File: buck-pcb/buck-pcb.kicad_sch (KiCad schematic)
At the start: 10 parts

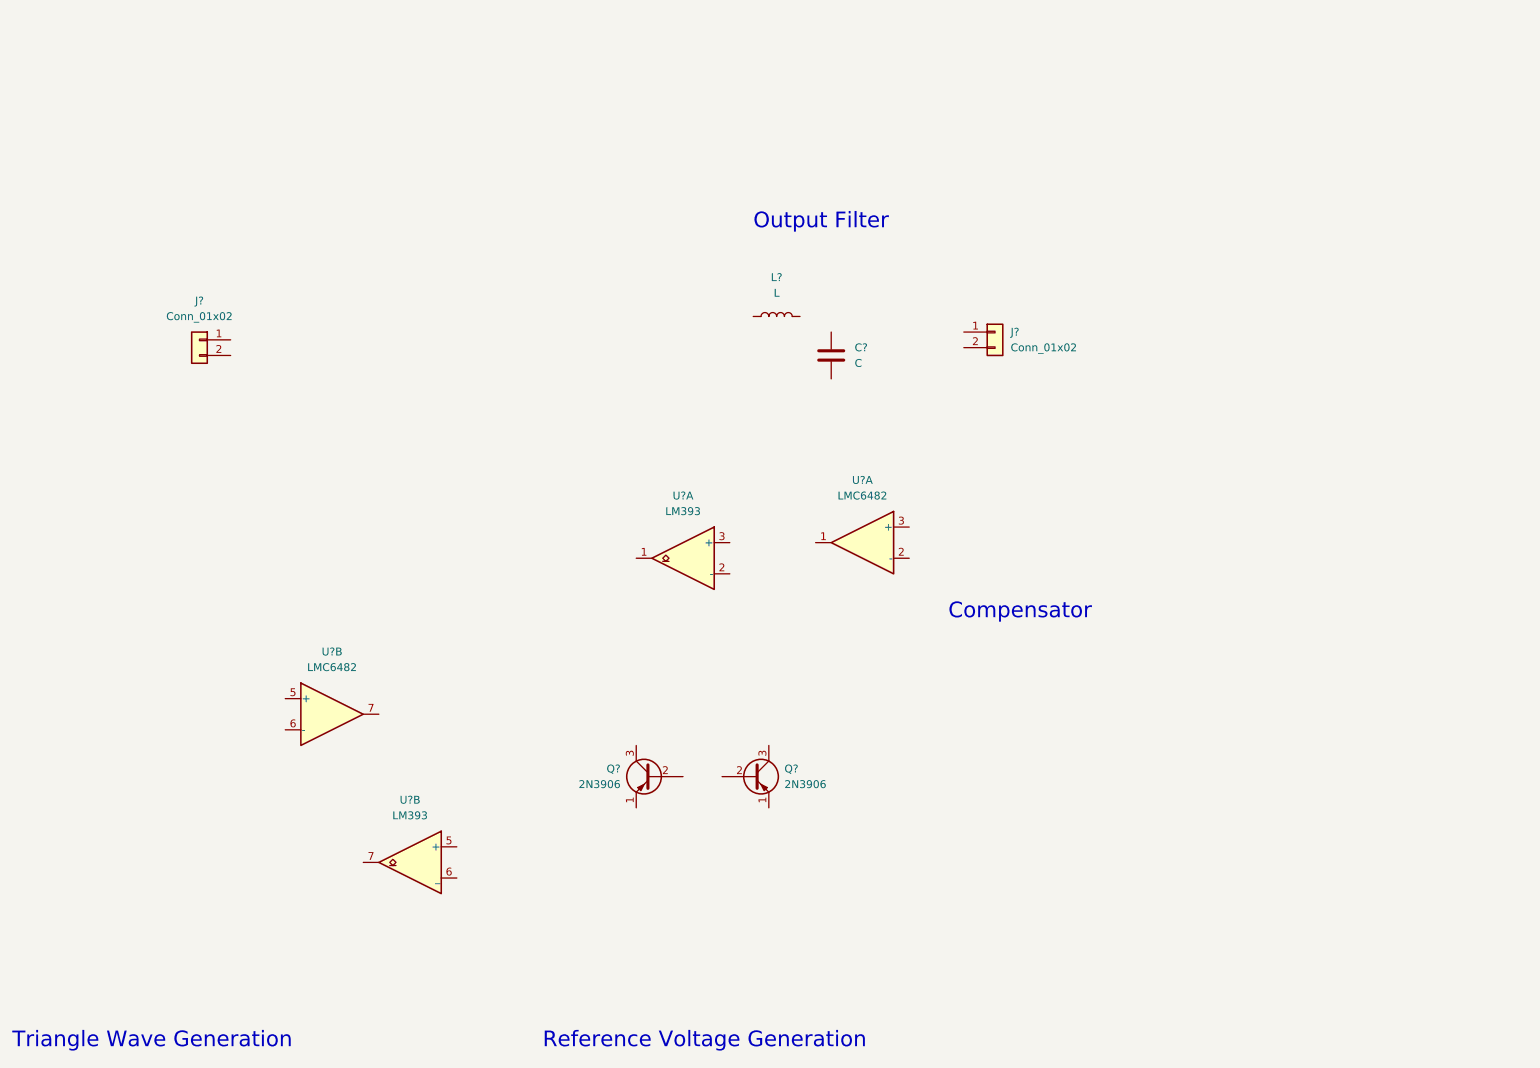
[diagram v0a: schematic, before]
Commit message: KiCAD schematic mostly done
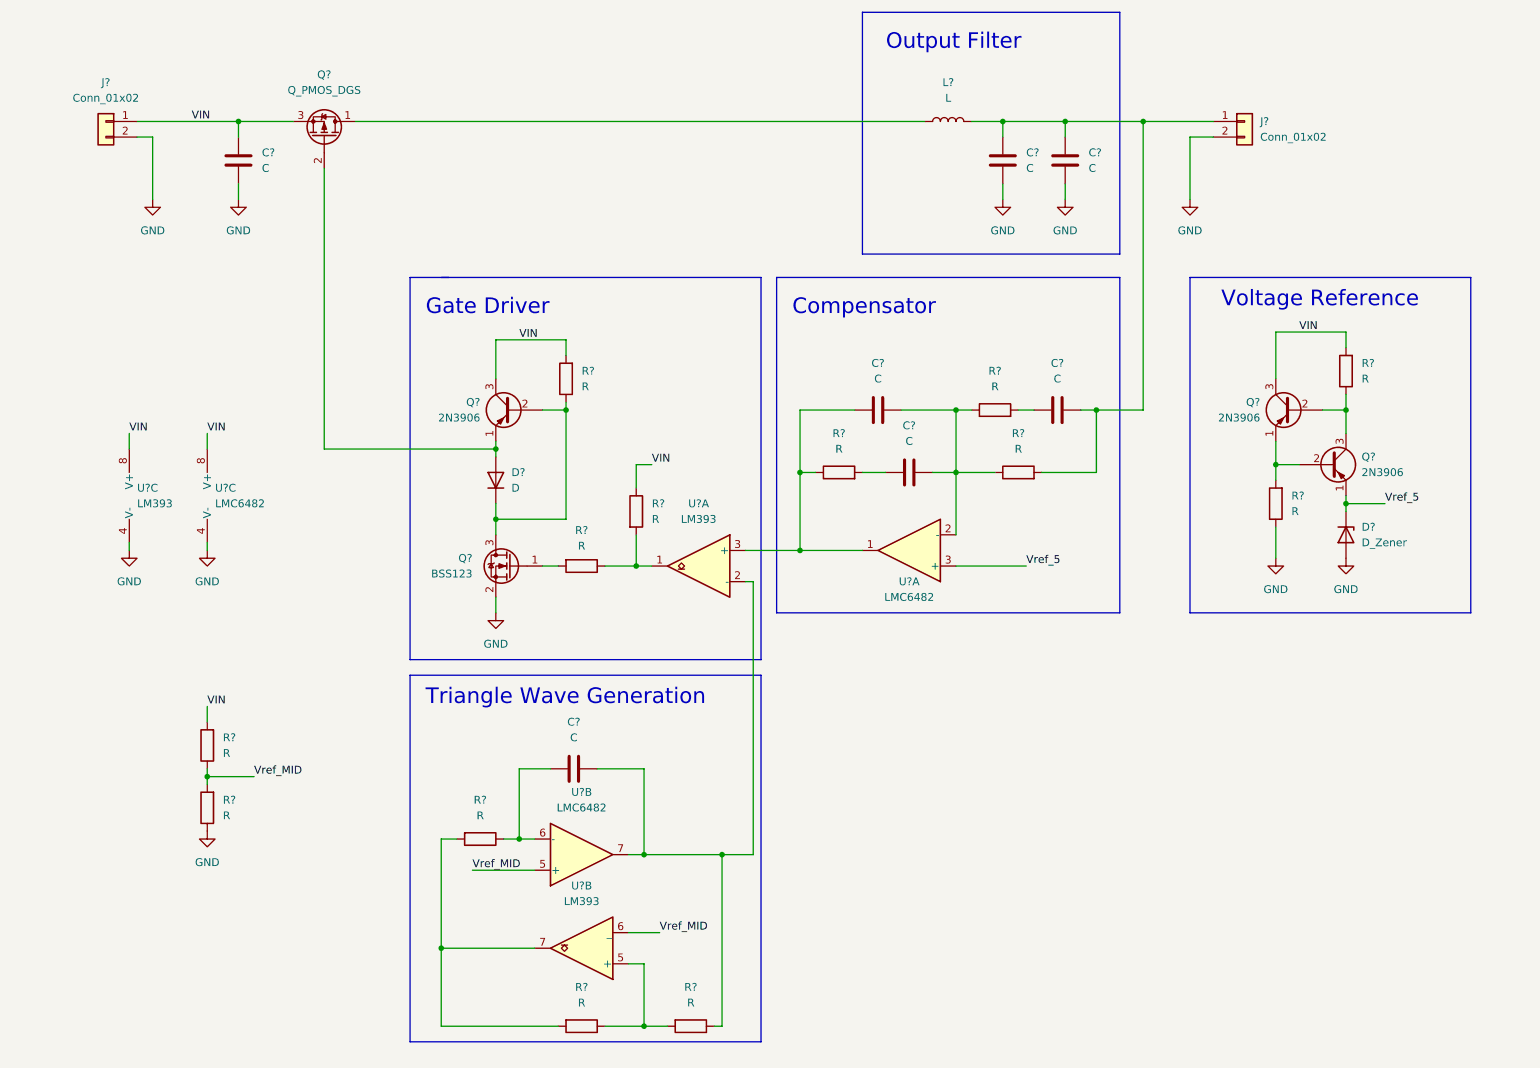
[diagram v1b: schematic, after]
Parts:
- removed Q? (x2): 2N3906, Package_TO_SOT_THT:TO-92_Inline, symbol Transistor_BJT:2N3906
- added C? (x6): C, symbol Device:C
- added D?: D_Zener, symbol Device:D_Zener
- added D?: D, symbol Device:D
- added Q? (x3): 2N3906, Package_TO_SOT_THT:TO-92_Inline, symbol Transistor_BJT:2N3906
- added Q?: Q_PMOS_DGS, symbol Device:Q_PMOS_DGS
- added Q?: BSS123, Package_TO_SOT_SMD:SOT-23, symbol Transistor_FET:BSS123
- added R? (x13): R, symbol Device:R
- added U?: LMC6482, symbol Amplifier_Operational:LMC6482
- added U?: LM393, symbol Comparator:LM393
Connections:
- net Vref_MID: now reaches U?.5 (+)
- net Vref_MID: now also U?.6 (_), R?.1, R?.2
- net at U?.6 (-): now also C?.1, R?.1
- net at U?.7: now also U?.2 (-), C?.2, R?.1
- net at U?.5 (+): now also R?.1, R?.2
- net at U?.7: now also R?.2, R?.2
- net at L?.1: now also Q?.1 (D)
- net at L?.2: now also C?.1, J?.1 (Pin_1), C?.1, C?.2, R?.2
- net at U?.1: now also U?.3 (+), C?.1, R?.1
- net at U?.2 (-): now also C?.2, C?.2, R?.1, R?.1
- net Vref_5: now reaches U?.3 (+)
- net Vref_5: now also D?.1 (K), Q?.1 (E)
- net GND: now reaches C?.2
- net GND: now also J?.2 (Pin_2), J?.2 (Pin_2), C?.2, C?.2, D?.2 (A), Q?.2 (S), R?.1, R?.1, U?.4 (V-), U?.4 (V-)
- net at U?.1: now also R?.1, R?.2
- net VIN: now reaches J?.1 (Pin_1)
- net VIN: now also C?.1, Q?.3 (C), Q?.3 (C), Q?.3 (S), R?.1, R?.2, R?.2, R?.2, U?.8 (V+), U?.8 (V+)
- new net: C?.1, R?.2 (x2)
- new net: Q?.1 (E), Q?.2 (B), R?.2
- new net: Q?.2 (B), Q?.3 (C), R?.1
- new net: D?.2 (A), Q?.1 (E), Q?.2 (G)
- new net: Q?.1 (G), R?.2
- new net: D?.1 (K), Q?.2 (B), Q?.3 (D), R?.1
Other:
- note added: "Gate Driver"
- note added: "Voltage Reference"
- note removed: "Reference Voltage Generation"
- moved on the sheet: C?, J?, L?, U?A, U?B

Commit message: Putting together complete system
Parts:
- added C? (x2): 0.1u, symbol Device:C
- added D?: D_Schottky, symbol Device:D_Schottky
- added R?: 270, symbol Device:R
- C1, C7: renamed from C?; value C -> 10u
- C2: renamed from C?; value C -> 200p
- C3: renamed from C?; value C -> 82p
- C4, C6: renamed from C?; value C -> 10n
- C5: renamed from C?; value C -> 100u
- R1, R12, R2, R8, R9: renamed from R?; value R -> 10k
- R10: renamed from R?; value R -> 680
- R11: renamed from R?; value R -> 27k
- R13: renamed from R?; value R -> 82
- R3: renamed from R?; value R -> 4.7k
- R4, R7: renamed from R?; value R -> 1k
- R5: renamed from R?; value R -> 33
- R6: renamed from R?; value R -> 20k
- gave numbers to parts that had none: 12
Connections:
- net GND: now also C?.2, C?.2, D?.2 (A)
- net VIN: now also C?.1, C?.1, R?.1
- net at L1.1, Q1.1 (D): now also D?.1 (K)
- net at R3.2, R6.2, U1.7: now also R?.2
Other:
- moved on the sheet: C2, C5, C7, L1, R1, R2, R3, R6, R8, U1B, U1C, U2B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

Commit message: FP assigned
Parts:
- removed Q1: Q_PMOS_DGS, symbol Device:Q_PMOS_DGS
- removed Q2, Q4, Q5: 2N3906, Package_TO_SOT_THT:TO-92_Inline, symbol Transistor_BJT:2N3906
- added D4: LED, LED_SMD:LED_0603_1608Metric, symbol Device:LED
- added Q1: Q_PMOS_GSD, Package_TO_SOT_SMD:SOT-23, symbol Device:Q_PMOS_GSD
- added Q2, Q4, Q5: MMBT3906, Package_TO_SOT_SMD:SOT-23, symbol Transistor_BJT:MMBT3906
- added R15: 270, Resistor_SMD:R_0603_1608Metric, symbol Device:R
- C1, C2, C3, C4, C6, C7: footprint (none) -> Capacitor_SMD:C_0603_1608Metric
- C5: footprint (none) -> Capacitor_THT:CP_Radial_D8.0mm_P3.50mm
- C8, C9: renamed from C?; footprint (none) -> Capacitor_SMD:C_0603_1608Metric
- D1: value D -> 1N4148; footprint (none) -> Diode_SMD:D_SOD-323_HandSoldering
- D2: footprint (none) -> Diode_THT:D_DO-41_SOD81_P7.62mm_Horizontal
- D3: renamed from D?; footprint (none) -> Diode_SMD:D_SMB
- J1, J2: footprint (none) -> Connector_PinHeader_2.54mm:PinHeader_1x02_P2.54mm_Vertical
- L1: value L -> 10u; footprint (none) -> Inductor_SMD:L_7.3x7.3_H3.5
- R1, R10, R11, R12, R13, R2, R3, R4, R5, R6, R7, R8, R9: footprint (none) -> Resistor_SMD:R_0603_1608Metric
- R14: renamed from R?; footprint (none) -> Resistor_SMD:R_0603_1608Metric
- U1, U2: footprint (none) -> Package_SO:SOIC-8_3.9x4.9mm_P1.27mm
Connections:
- net GND: now also D4.1 (K)
- net VIN: now also Q1.2 (S), Q2.3 (C), Q4.3 (C)
- net Vref_5: now also Q5.2 (E)
- net at C5.1, C6.2, C7.1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: now also R15.1
- net at R12.2: now also Q4.2 (E), Q5.1 (B)
- net at R13.1: now also Q4.1 (B), Q5.3 (C)
- net at D3.1 (K), L1.1: now also Q1.3 (D)
- net at D1.2 (A): now also Q1.1 (G), Q2.2 (E)
- net at D1.1 (K), Q3.3 (D), R4.1: now also Q2.1 (B)
- new net: D4.2 (A), R15.2
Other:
- moved on the sheet: J2

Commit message: Initial layout
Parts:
- added C10: 0.1u, Capacitor_SMD:C_0603_1608Metric, symbol Device:C
- D2: footprint Diode_THT:D_DO-41_SOD81_P7.62mm_Horizontal -> Diode_SMD:D_SOD-123
- L1: footprint Inductor_SMD:L_7.3x7.3_H3.5 -> buck-graphics:BMRx00060630
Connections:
- net GND: now also C10.2
- net Vref_5: now also U2.5 (+); no longer U2.3 (+)
- net Vref_MID: now also U2.3 (+), C10.1; no longer U2.5 (+)
- net VOUT: now reaches C5.1, C6.2, C7.1, J2.1 (Pin_1), L1.2, R11.2, R15.1
- net at C3.2, C4.2, R10.1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: now also U2.6 (-); no longer U2.2 (-)
- net at C3.1, R9.1, U1.3 (+): now also U2.7; no longer U2.1
- net at C2.1, R3.1: now also U2.2 (-); no longer U2.6 (-)
- net at C2.2, R8.1, U1.2 (-): now also U2.1; no longer U2.7
- net VSW: now reaches D3.1 (K), L1.1, Q1.3 (D)
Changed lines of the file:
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@@
   (junction (at 234.95 102.87) (diameter 0) (color 0 0 0 0)
   )
+  (junction (at 50.8 152.4) (diameter 0) (color 0 0 0 0)
+  )
   (junction (at 96.52 105.41) (diameter 0) (color 0 0 0 0)
   )
@@
     (stroke (width 0) (type default) (color 0 0 0 0))
   )
+  (wire (pts (xy 50.8 152.4) (xy 39.37 152.4))
+    (stroke (width 0) (type default) (color 0 0 0 0))
+  )
   (wire (pts (xy 96.52 105.41) (xy 96.52 107.95))
     (stroke (width 0) (type default) (color 0 0 0 0))
@@
     (stroke (width 0) (type default) (color 0 0 0 0))
   )
+  (wire (pts (xy 50.8 152.4) (xy 50.8 153.67))
+    (stroke (width 0) (type default) (color 0 0 0 0))
+  )
   (wire (pts (xy 201.93 40.64) (xy 201.93 87.63))
     (stroke (width 0) (type default) (color 0 0 0 0))
@@
     (stroke (width 0) (type default) (color 0 0 0 0))
   )
-  (wire (pts (xy 46.99 152.4) (xy 39.37 152.4))
+  (wire (pts (xy 53.34 152.4) (xy 50.8 152.4))
     (stroke (width 0) (type default) (color 0 0 0 0))
   )
@@
     (effects (font (size 2.54 2.54)) (justify left bottom))
   )
+  (label "VSW" (at 120.65 40.64 0)
+    (effects (font (size 1.27 1.27)) (justify left bottom))
+  )
   (label "VIN" (at 33.02 105.41 0)
     (effects (font (size 1.27 1.27)) (justify left bottom))
@@
     (effects (font (size 1.27 1.27)) (justify left bottom))
   )
+  (label "VOUT" (at 227.33 40.64 0)
+    (effects (font (size 1.27 1.27)) (justify left bottom))
+  )
   (label "VIN" (at 39.37 140.97 0)
     (effects (font (size 1.27 1.27)) (justify left bottom))
@@
     (effects (font (size 1.27 1.27)) (justify left bottom))
   )
-  (label "Vref_MID" (at 46.99 152.4 0)
+  (label "Vref_MID" (at 53.34 152.4 0)
     (effects (font (size 1.27 1.27)) (justify left bottom))
   )
@@
     (pin "2")
   )
+  (symbol (lib_id "Device:C") (at 50.8 157.48 0) (unit 1)
+    (in_bom yes) (on_board yes) (fields_autoplaced)
+    (property "Reference" "C10" (id 0) (at 54.61 156.2099 0)
+      (effects (font (size 1.27 1.27)) (justify left))
+    )
+    (property "Value" "0.1u" (id 1) (at 54.61 158.7499 0)
+      (effects (font (size 1.27 1.27)) (justify left))
+    )
+    (property "Footprint" "Capacitor_SMD:C_0603_1608Metric" (id 2) (at 51.7652 161.29 0)
+      (effects (font (size 1.27 1.27)) hide)
+    )
+    (property "Datasheet" "~" (id 3) (at 50.8 157.48 0)
+      (effects (font (size 1.27 1.27)) hide)
+    )
+    (pin "1")
+    (pin "2")
+  )
   (symbol (lib_id "Device:C") (at 187.96 46.99 0) (unit 1)
     (in_bom yes) (on_board yes) (fields_autoplaced)
@@
     (pin "1")
   )
-  (symbol (lib_id "Amplifier_Operational:LMC6482") (at 110.49 161.29 0) (mirror x) (unit 2)
+  (symbol (lib_id "Amplifier_Operational:LMC6482") (at 110.49 161.29 0) (mirror x) (unit 1)
     (in_bom yes) (on_board yes)
     (property "Reference" "U2" (id 0) (at 114.3 153.67 0))
@@
       (effects (font (size 1.27 1.27)) hide)
     )
-    (pin "5")
-    (pin "6")
-    (pin "7")
+    (pin "1")
+    (pin "2")
+    (pin "3")
   )
   (symbol (lib_id "power:GND") (at 54.61 53.34 0) (unit 1)
@@
     (property "Reference" "L1" (id 0) (at 166.37 34.29 90))
     (property "Value" "10u" (id 1) (at 166.37 36.83 90))
-    (property "Footprint" "Inductor_SMD:L_7.3x7.3_H3.5" (id 2) (at 166.37 40.64 0)
+    (property "Footprint" "buck-graphics:BMRx00060630" (id 2) (at 166.37 40.64 0)
       (effects (font (size 1.27 1.27)) hide)
     )
@@
     (pin "1")
   )
-  (symbol (lib_id "Amplifier_Operational:LMC6482") (at 163.83 110.49 180) (unit 1)
+  (symbol (lib_id "Amplifier_Operational:LMC6482") (at 163.83 110.49 180) (unit 2)
     (in_bom yes) (on_board yes)
     (property "Reference" "U2" (id 0) (at 163.83 115.57 0))
@@
       (effects (font (size 1.27 1.27)) hide)
     )
-    (pin "1")
-    (pin "2")
-    (pin "3")
+    (pin "5")
+    (pin "6")
+    (pin "7")
   )
   (symbol (lib_id "power:GND") (at 46.99 118.11 0) (unit 1)
@@
     (pin "2")
   )
+  (symbol (lib_id "power:GND") (at 50.8 161.29 0) (unit 1)
+    (in_bom yes) (on_board yes) (fields_autoplaced)
+    (property "Reference" "#PWR0101" (id 0) (at 50.8 167.64 0)
+      (effects (font (size 1.27 1.27)) hide)
+    )
+    (property "Value" "GND" (id 1) (at 50.8 166.37 0))
+    (property "Footprint" "" (id 2) (at 50.8 161.29 0)
+      (effects (font (size 1.27 1.27)) hide)
+    )
+    (property "Datasheet" "" (id 3) (at 50.8 161.29 0)
+      (effects (font (size 1.27 1.27)) hide)
+    )
+    (pin "1")
+  )
   (symbol (lib_id "power:GND") (at 33.02 118.11 0) (unit 1)
     (in_bom yes) (on_board yes) (fields_autoplaced)
@@
       (effects (font (size 1.27 1.27)) (justify left))
     )
-    (property "Footprint" "Diode_THT:D_DO-41_SOD81_P7.62mm_Horizontal" (id 2) (at 234.95 107.95 0)
+    (property "Footprint" "Diode_SMD:D_SOD-123" (id 2) (at 234.95 107.95 0)
       (effects (font (size 1.27 1.27)) hide)
     )
@@
       (reference "#PWR015") (unit 1) (value "GND") (footprint "")
     )
+    (path "/cd9f7193-c134-4e35-b550-bcfe2155c88e"
+      (reference "#PWR0101") (unit 1) (value "GND") (footprint "")
+    )
     (path "/30d31727-8e0f-449d-aa6e-ffb0c66bd448"
       (reference "C1") (unit 1) (value "10u") (footprint "Capacitor_SMD:C_0603_1608Metric")
@@
       (reference "C9") (unit 1) (value "0.1u") (footprint "Capacitor_SMD:C_0603_1608Metric")
     )
+    (path "/207f3b04-5d05-4d5e-a65c-613b60a18274"
+      (reference "C10") (unit 1) (value "0.1u") (footprint "Capacitor_SMD:C_0603_1608Metric")
+    )
     (path "/eb146731-2879-4699-bc00-e8e6010b77ab"
       (reference "D1") (unit 1) (value "1N4148") (footprint "Diode_SMD:D_SOD-323_HandSoldering")
     )
     (path "/d7ea3f33-f308-4721-81bb-746244b64807"
-      (reference "D2") (unit 1) (value "D_Zener") (footprint "Diode_THT:D_DO-41_SOD81_P7.62mm_Horizontal")
+      (reference "D2") (unit 1) (value "D_Zener") (footprint "Diode_SMD:D_SOD-123")
     )
     (path "/aae01ab9-176d-45dc-8846-cc715be406a0"
@@
     )
     (path "/7a7be03b-d30a-4fc6-abe7-e94916bf3a0b"
-      (reference "L1") (unit 1) (value "10u") (footprint "Inductor_SMD:L_7.3x7.3_H3.5")
+      (reference "L1") (unit 1) (value "10u") (footprint "buck-graphics:BMRx00060630")
     )
     (path "/c70c6b42-076d-480e-b33c-459aff21d426"
@@
       (reference "U1") (unit 3) (value "LM393") (footprint "Package_SO:SOIC-8_3.9x4.9mm_P1.27mm")
     )
+    (path "/59b769a2-11ff-47ac-ab14-6ab002bc58dc"
+      (reference "U2") (unit 1) (value "LMC6482") (footprint "Package_SO:SOIC-8_3.9x4.9mm_P1.27mm")
+    )
     (path "/8e96f4d0-8f69-48d9-84bc-1dc2d0486888"
-      (reference "U2") (unit 1) (value "LMC6482") (footprint "Package_SO:SOIC-8_3.9x4.9mm_P1.27mm")
-    )
-    (path "/59b769a2-11ff-47ac-ab14-6ab002bc58dc"
       (reference "U2") (unit 2) (value "LMC6482") (footprint "Package_SO:SOIC-8_3.9x4.9mm_P1.27mm")
     )

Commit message: Gerbers sent
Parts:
- added TP1: TestPoint, TestPoint:TestPoint_Keystone_5005-5009_Compact, symbol Connector:TestPoint
- C5: footprint Capacitor_THT:CP_Radial_D8.0mm_P3.50mm -> Capacitor_SMD:CP_Elec_6.3x4.9
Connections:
- net GND: now also TP1.1
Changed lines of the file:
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@@
     (pin "2")
+  )
+  (symbol (lib_id "power:GND") (at 39.37 177.8 0) (unit 1)
+    (in_bom yes) (on_board yes) (fields_autoplaced)
+    (property "Reference" "#PWR016" (id 0) (at 39.37 184.15 0)
+      (effects (font (size 1.27 1.27)) hide)
+    )
+    (property "Value" "GND" (id 1) (at 39.37 182.88 0))
+    (property "Footprint" "" (id 2) (at 39.37 177.8 0)
+      (effects (font (size 1.27 1.27)) hide)
+    )
+    (property "Datasheet" "" (id 3) (at 39.37 177.8 0)
+      (effects (font (size 1.27 1.27)) hide)
+    )
+    (pin "1")
   )
   (symbol (lib_id "Device:R") (at 110.49 113.03 270) (unit 1)
@@
     (pin "1")
     (pin "2")
+  )
+  (symbol (lib_id "Connector:TestPoint") (at 39.37 177.8 0) (unit 1)
+    (in_bom yes) (on_board yes) (fields_autoplaced)
+    (property "Reference" "TP1" (id 0) (at 41.91 173.2279 0)
+      (effects (font (size 1.27 1.27)) (justify left))
+    )
+    (property "Value" "TestPoint" (id 1) (at 41.91 175.7679 0)
+      (effects (font (size 1.27 1.27)) (justify left))
+    )
+    (property "Footprint" "TestPoint:TestPoint_Keystone_5005-5009_Compact" (id 2) (at 44.45 177.8 0)
+      (effects (font (size 1.27 1.27)) hide)
+    )
+    (property "Datasheet" "~" (id 3) (at 44.45 177.8 0)
+      (effects (font (size 1.27 1.27)) hide)
+    )
+    (pin "1")
   )
   (symbol (lib_id "power:GND") (at 223.52 111.76 0) (unit 1)
@@
       (effects (font (size 1.27 1.27)) (justify left))
     )
-    (property "Footprint" "Capacitor_THT:CP_Radial_D8.0mm_P3.50mm" (id 2) (at 176.2252 50.8 0)
+    (property "Footprint" "Capacitor_SMD:CP_Elec_6.3x4.9" (id 2) (at 176.2252 50.8 0)
       (effects (font (size 1.27 1.27)) hide)
     )
@@
       (reference "#PWR015") (unit 1) (value "GND") (footprint "")
     )
+    (path "/3f225173-691b-4ada-b9a0-d77b32c03fda"
+      (reference "#PWR016") (unit 1) (value "GND") (footprint "")
+    )
     (path "/cd9f7193-c134-4e35-b550-bcfe2155c88e"
       (reference "#PWR0101") (unit 1) (value "GND") (footprint "")
@@
     )
     (path "/a94c856f-aa13-433f-9f44-bd4724bec9ed"
-      (reference "C5") (unit 1) (value "100u") (footprint "Capacitor_THT:CP_Radial_D8.0mm_P3.50mm")
+      (reference "C5") (unit 1) (value "100u") (footprint "Capacitor_SMD:CP_Elec_6.3x4.9")
     )
     (path "/03086bd2-7804-4401-a56e-730bf06bdb2e"
@@
       (reference "R15") (unit 1) (value "270") (footprint "Resistor_SMD:R_0603_1608Metric")
     )
+    (path "/545ca384-b26e-43be-8c78-25a5055751b8"
+      (reference "TP1") (unit 1) (value "TestPoint") (footprint "TestPoint:TestPoint_Keystone_5005-5009_Compact")
+    )
     (path "/c763810b-d6a0-42c7-a6cc-22f9b0524543"
